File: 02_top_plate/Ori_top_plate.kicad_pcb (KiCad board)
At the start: 2 copper layers, 227.2 x 75.2 mm, 62 parts, among them U1 HOLE, U10 HOLE, U11 HOLE, U12 HOLE, U13 HOLE, U14 HOLE, U15 HOLE, U16 HOLE, U17 HOLE, U18 HOLE, U19 HOLE, U2 HOLE, U20 HOLE, U21 HOLE, U22 HOLE, U23 HOLE, U24 HOLE, U25 HOLE, U26 HOLE, U27 HOLE, U28 HOLE, U29 HOLE, U3 HOLE, U30 HOLE, U31 HOLE, U32 HOLE, U33 HOLE, U34 HOLE, U35 HOLE, U36 HOLE, U37 HOLE, U38 HOLE, U39 HOLE, U4 HOLE, U40 HOLE, U41 HOLE, U42 HOLE, U43 HOLE, U44 HOLE, U45 HOLE, U46 HOLE, U47 HOLE, U48 HOLE, U5 HOLE, U6 HOLE, U7 HOLE, U8 HOLE, U9 HOLE

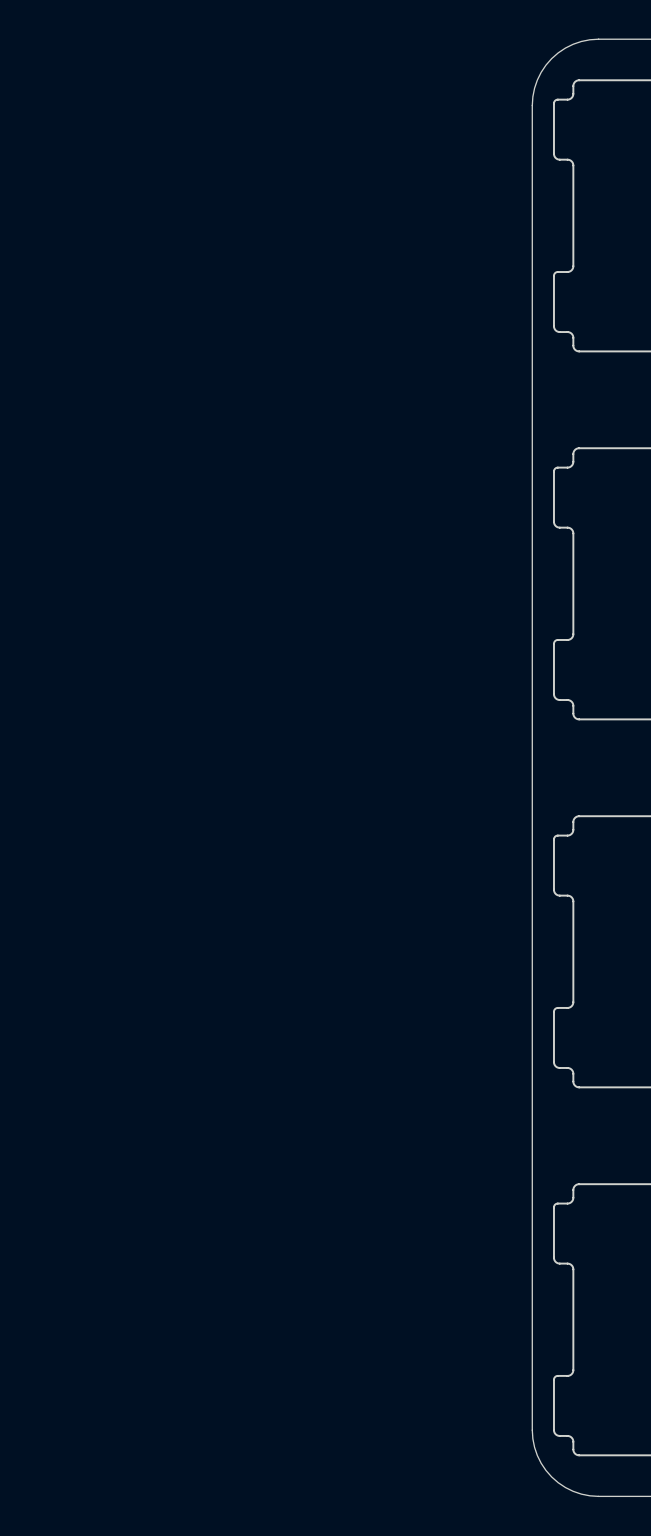
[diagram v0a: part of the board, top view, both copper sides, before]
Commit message: update
added macro column to top plate
re-routed some traces
new previews
removed some ground plane
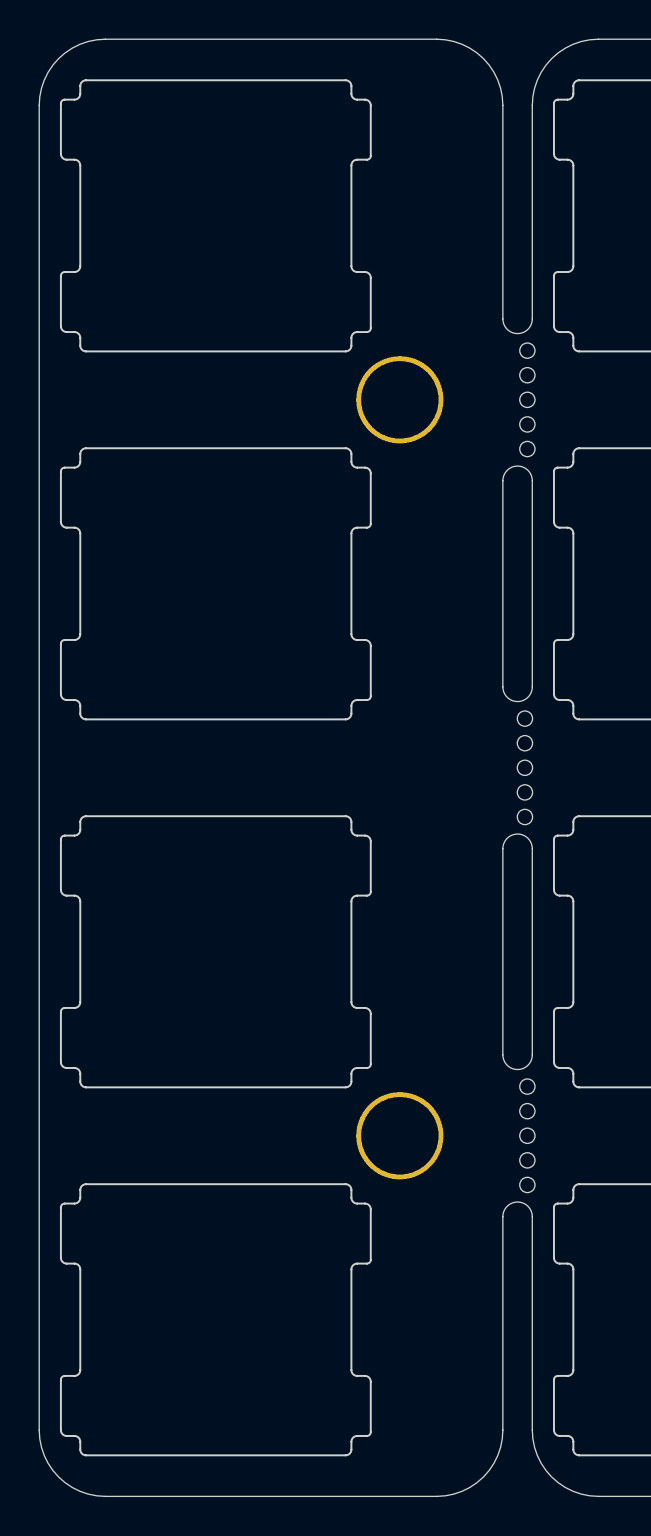
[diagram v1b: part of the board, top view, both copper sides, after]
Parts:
- added H15: MountingHole, random-keyboard-parts:plate_hole_4mm_tht, F.Cu at (124.6, 63.2)
- added H16: MountingHole, random-keyboard-parts:plate_hole_4mm_tht, F.Cu at (124.6, 101.2)
- added H17: MountingHole, random-keyboard-parts:breakaway-mousebites, F.Cu at (131.5, 99.2)
- added H18: MountingHole, random-keyboard-parts:breakaway-mousebites, F.Cu at (131.4, 80.2)
- added H19: MountingHole, random-keyboard-parts:breakaway-mousebites, F.Cu at (131.5, 61.2)
- added U49: HOLE, random-keyboard-parts:MX100_slot, F.Cu at (115.1, 51.7)
- added U50: HOLE, random-keyboard-parts:MX100_slot, F.Cu at (115.1, 70.7)
- added U51: HOLE, random-keyboard-parts:MX100_slot, F.Cu at (115.1, 89.7)
- added U52: HOLE, random-keyboard-parts:MX100_slot, F.Cu at (115.1, 108.7)
- renumbered H14 to H1, H2 to H10, H3 to H11, H6 to H12, H4 to H13, H5 to H14, H15 to H2, H11 to H3, H12 to H4, H13 to H5, H16 to H6, H17 to H7, H18 to H8, H1 to H9
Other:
- board size 227.2 x 75.2 mm -> 252.7 x 75.2 mm

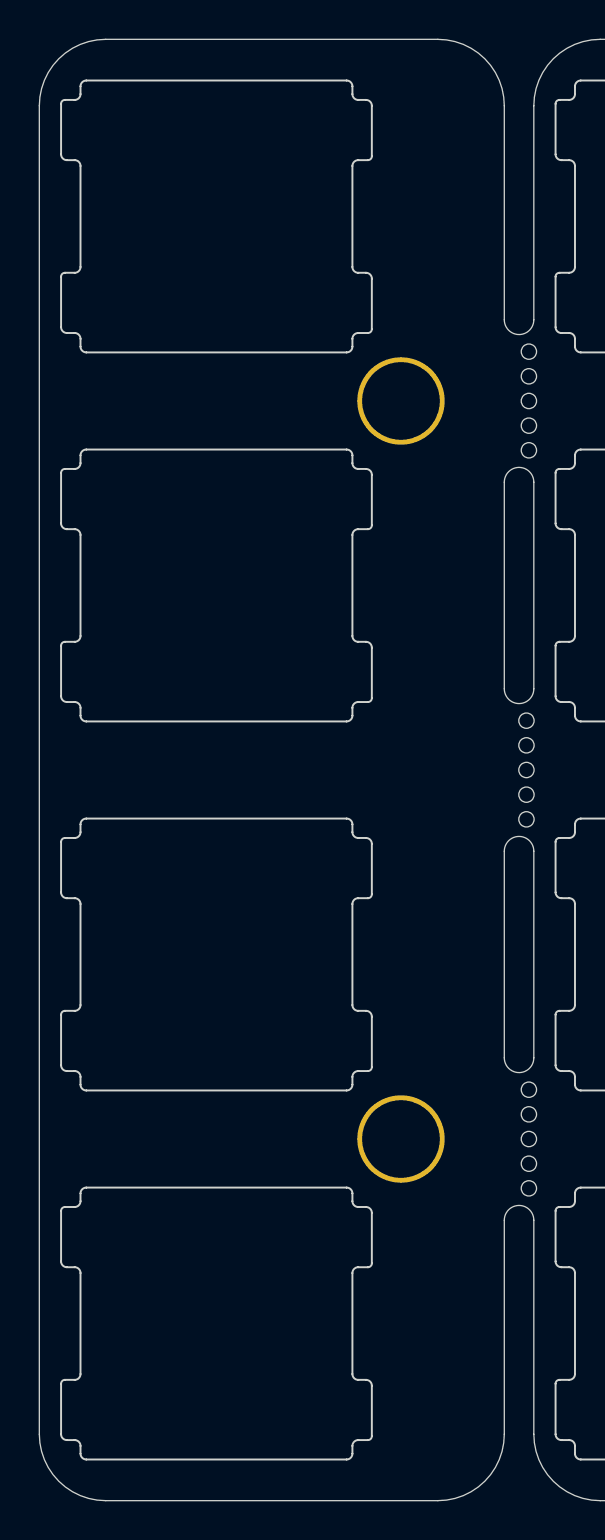
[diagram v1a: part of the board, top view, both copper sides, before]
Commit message: Moved macro column a tiny bit
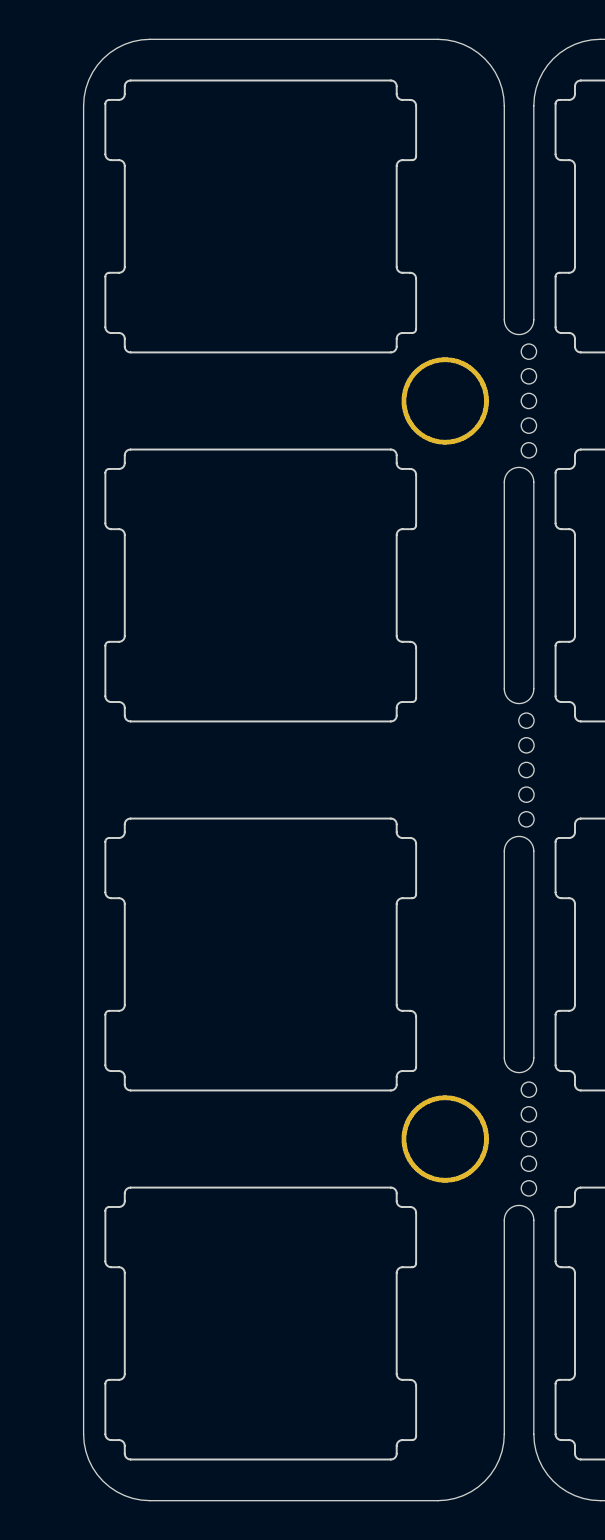
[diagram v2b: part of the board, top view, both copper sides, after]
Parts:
- moved U49 2.28 mm to (117.4, 51.7)
- moved U50 2.28 mm to (117.4, 70.7)
- moved U51 2.28 mm to (117.4, 89.7)
- moved U52 2.28 mm to (117.4, 108.7)
- moved H15 2.28 mm to (126.9, 63.2)
- moved H16 2.28 mm to (126.9, 101.2)
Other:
- board size 252.7 x 75.2 mm -> 250.4 x 75.2 mm
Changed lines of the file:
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@@
   (general
     (thickness 1.6)
-    (drawings 32)
+    (drawings 33)
     (tracks 0)
     (zones 0)
@@
   )
   (module random-keyboard-parts:MX100_slot (layer F.Cu)
-    (at 115.14 108.68)
+    (at 117.419994 108.68)
     (fp_text reference U52 (at 0.0127 1.8288) (layer Dwgs.User)
       (effects (font (size 1 1) (thickness 0.15)))
@@
   )
   (module random-keyboard-parts:MX100_slot (layer F.Cu)
-    (at 115.14 89.68)
+    (at 117.419994 89.68)
     (fp_text reference U51 (at 0.0127 1.8288) (layer Dwgs.User)
       (effects (font (size 1 1) (thickness 0.15)))
@@
   )
   (module random-keyboard-parts:MX100_slot (layer F.Cu)
-    (at 115.14 70.68)
+    (at 117.419994 70.68)
     (fp_text reference U50 (at 0.0127 1.8288) (layer Dwgs.User)
       (effects (font (size 1 1) (thickness 0.15)))
@@
   )
   (module random-keyboard-parts:MX100_slot (layer F.Cu)
-    (at 115.14 51.68)
+    (at 117.419994 51.68)
     (fp_text reference U49 (at 0.0127 1.8288) (layer Dwgs.User)
       (effects (font (size 1 1) (thickness 0.15)))
@@
   )
   (module random-keyboard-parts:plate_hole_4mm_tht (layer F.Cu)
-    (at 124.5892 101.212)
+    (at 126.868866 101.212)
     (fp_text reference H16 (at 0.381 1.4097) (layer Dwgs.User)
       (effects (font (size 1 1) (thickness 0.15)))
@@
   )
   (module random-keyboard-parts:plate_hole_4mm_tht (layer F.Cu)
-    (at 124.5892 63.212)
+    (at 126.868866 63.211839)
     (fp_text reference H15 (at 0.381 1.4097) (layer Dwgs.User)
       (effects (font (size 1 1) (thickness 0.15)))
@@
     (pad 1 thru_hole circle (at 0.0508 -2.032) (size 4.5 4.5) (drill 4) (layers *.Cu *.Mask))
   )
-  (gr_line (start 126.54 117.8) (end 109.44 117.8) (layer Edge.Cuts) (width 0.05))
+  (dimension 4.129636 (width 0.15) (layer Dwgs.User)
+    (gr_text "0.1626 in" (at 129.009495 32.519843 0.001886903836) (layer Dwgs.User)
+      (effects (font (size 1 1) (thickness 0.15)))
+    )
+    (feature1 (pts (xy 126.944994 42.155) (xy 126.9447 33.23349)))
+    (feature2 (pts (xy 131.07463 42.154864) (xy 131.074336 33.233354)))
+    (crossbar (pts (xy 131.074356 33.819775) (xy 126.94472 33.819911)))
+    (arrow1a (pts (xy 126.94472 33.819911) (xy 128.071204 33.233453)))
+    (arrow1b (pts (xy 126.94472 33.819911) (xy 128.071243 34.406295)))
+    (arrow2a (pts (xy 131.074356 33.819775) (xy 129.947833 33.233391)))
+    (arrow2b (pts (xy 131.074356 33.819775) (xy 129.947872 34.406233)))
+  )
+  (dimension 4.129636 (width 0.15) (layer Dwgs.User)
+    (gr_text "4.130 mm" (at 129.009632 36.699832 0.001886903836) (layer Dwgs.User)
+      (effects (font (size 1 1) (thickness 0.15)))
+    )
+    (feature1 (pts (xy 126.944994 42.155) (xy 126.944838 37.413479)))
+    (feature2 (pts (xy 131.07463 42.154864) (xy 131.074474 37.413343)))
+    (crossbar (pts (xy 131.074493 37.999764) (xy 126.944857 37.9999)))
+    (arrow1a (pts (xy 126.944857 37.9999) (xy 128.071341 37.413442)))
+    (arrow1b (pts (xy 126.944857 37.9999) (xy 128.07138 38.586284)))
+    (arrow2a (pts (xy 131.074493 37.999764) (xy 129.94797 37.41338)))
+    (arrow2b (pts (xy 131.074493 37.999764) (xy 129.948009 38.586222)))
+  )
+  (gr_line (start 126.54 117.8) (end 111.719994 117.8) (layer Edge.Cuts) (width 0.05))
   (gr_line (start 129.96 114.38) (end 129.96 103.36) (layer Edge.Cuts) (width 0.05))
   (gr_arc (start 126.54 114.38) (end 126.54 117.8) (angle -90) (layer Edge.Cuts) (width 0.05))
@@
   (gr_line (start 129.96 45.98) (end 129.96 57) (layer Edge.Cuts) (width 0.05))
   (gr_line (start 131.48 45.98) (end 131.48 57) (layer Edge.Cuts) (width 0.05))
-  (gr_line (start 126.54 42.56) (end 109.44 42.56) (layer Edge.Cuts) (width 0.05))
+  (gr_line (start 126.54 42.56) (end 111.719994 42.56) (layer Edge.Cuts) (width 0.05))
   (gr_arc (start 130.72 57) (end 129.96 57) (angle -180) (layer Edge.Cuts) (width 0.05))
   (gr_arc (start 126.54 45.98) (end 129.96 45.98) (angle -90) (layer Edge.Cuts) (width 0.05))
-  (gr_line (start 106.02 45.98) (end 106.02 114.38) (layer Edge.Cuts) (width 0.05))
-  (gr_arc (start 109.44 45.98) (end 109.44 42.56) (angle -90) (layer Edge.Cuts) (width 0.05))
-  (gr_arc (start 109.44 114.38) (end 106.02 114.38) (angle -90) (layer Edge.Cuts) (width 0.05))
-  (dimension 6.40963 (width 0.15) (layer Cmts.User)
-    (gr_text "0.2523 in" (at 127.869691 36.31994 0.001215706057) (layer Cmts.User)
-      (effects (font (size 1 1) (thickness 0.15)))
-    )
-    (feature1 (pts (xy 124.665 42.155) (xy 124.664891 37.033587)))
-    (feature2 (pts (xy 131.07463 42.154864) (xy 131.074521 37.033451)))
-    (crossbar (pts (xy 131.074534 37.619872) (xy 124.664904 37.620008)))
-    (arrow1a (pts (xy 124.664904 37.620008) (xy 125.791395 37.033563)))
-    (arrow1b (pts (xy 124.664904 37.620008) (xy 125.79142 38.206405)))
-    (arrow2a (pts (xy 131.074534 37.619872) (xy 129.948018 37.033475)))
-    (arrow2b (pts (xy 131.074534 37.619872) (xy 129.948043 38.206317)))
-  )
+  (gr_line (start 108.299994 45.98) (end 108.299994 114.38) (layer Edge.Cuts) (width 0.05))
+  (gr_arc (start 111.719994 45.98) (end 111.719994 42.56) (angle -90) (layer Edge.Cuts) (width 0.05))
+  (gr_arc (start 111.719994 114.38) (end 108.299994 114.38) (angle -90) (layer Edge.Cuts) (width 0.05))
   (gr_text github.com/dierickdie (at 245.099355 61.179839) (layer B.SilkS)
     (effects (font (size 1.5 1.5) (thickness 0.2)) (justify mirror))

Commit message: 19.05mm spacing; move macro column to right side
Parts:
- removed H10, H11, H12, H13, H14, H9: MountingHole, random-keyboard-parts:plate_hole_4mm_tht
- added D1: DIODE, Diode_SMD:D_0603_1608Metric_Pad1.05x0.95mm_HandSolder, B.Cu at (374.5, 60.7)
- added D2: DIODE, Diode_SMD:D_0603_1608Metric_Pad1.05x0.95mm_HandSolder, B.Cu at (350.0, 60.7)
- moved U49 256.4 mm to (373.9, 51.2)
- moved U50 256.4 mm to (373.9, 70.2)
- moved U51 256.4 mm to (373.9, 89.3)
- moved U52 256.4 mm to (373.9, 108.3)
- moved H15 237.4 mm to (364.3, 62.8)
- moved H16 237.4 mm to (364.3, 100.9)
- moved H18 227.9 mm to (359.2, 79.8)
- moved H19 227.7 mm to (359.2, 60.7)
- moved H17 227.7 mm to (359.2, 98.8)
- moved U12 0.66 mm to (350.0, 51.2)
- moved U11 0.62 mm to (331.0, 51.2)
- moved U24 0.62 mm to (350.0, 70.2)
- moved H7 0.62 mm to (340.5, 62.8)
- moved U10 0.59 mm to (311.9, 51.2)
- moved U36 0.59 mm to (350.0, 89.3)
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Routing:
- net GNDA: track 0.00 -> 1.51 mm, vias 0 -> 1
- net GND: track 0.00 -> 1.51 mm, vias 0 -> 1
- added copper zone on B.Cu, net GND
- added copper zone on F.Cu, net GND
- added copper zone on B.Cu, net GNDA
- added copper zone on F.Cu, net GNDA
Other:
- board size 250.4 x 75.2 mm -> 251.2 x 75 mm

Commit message: updated plate holes
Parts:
- H17, H18, H19: footprint random-keyboard-parts:breakaway-mousebites -> Keeb_footprints:MouseBite_IPC7351
- U1, U10, U11, U12, U13, U14, U15, U16, U17, U18, U19, U2, U20, U21, U22, U23, U24, U25, U26, U27, U28, U29, U3, U30, U31, U32, U33, U34, U35, U36, U37, U38, U39, U4, U40, U41, U42, U43, U44, U45, U46, U47, U48, U49, U5, U50, U51, U52, U6, U7, U8, U9: footprint random-keyboard-parts:MX100_slot -> Keebio-Parts:MX_Switch_Cutout

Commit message: Updated firmware
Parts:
- removed H17: MountingHole, Keeb_footprints:MouseBite_IPC7351
- removed U50, U51, U52: HOLE, Keebio-Parts:MX_Switch_Cutout
- added H10: MountingHole, random-keyboard-parts:Generic-Mounthole, F.Cu at (222.6, 59.5)
- added H11: MountingHole, random-keyboard-parts:Generic-Mounthole, F.Cu at (222.6, 97.6)
- added H12: MountingHole, random-keyboard-parts:Generic-Mounthole, F.Cu at (297.9, 59.7)
- added H13: MountingHole, random-keyboard-parts:Generic-Mounthole, F.Cu at (298.8, 97.6)
- added H14: MountingHole, random-keyboard-parts:Generic-Mounthole, F.Cu at (356.0, 59.5)
- added H20: MountingHole, acheron_Hardware:MouseBite_IPC7351, F.Cu at (375.0, 78.6)
- added H21: MountingHole, random-keyboard-parts:Generic-Mounthole, F.Cu at (389.4, 39.9)
- added H22: MountingHole, random-keyboard-parts:Generic-Mounthole, F.Cu at (389.4, 117.3)
- added H9: MountingHole, random-keyboard-parts:Generic-Mounthole, F.Cu at (165.5, 59.5)
- added U53: HOLE, Keeb_footprints:MX100_slot, F.Cu at (389.4, 69.0)
- added U57: HOLE, Keeb_footprints:MX100_slot, F.Cu at (389.4, 88.1)
- added U61: HOLE, Keeb_footprints:MX100_slot, F.Cu at (389.3, 107.2)
- D1, D2: footprint Diode_SMD:D_0603_1608Metric_Pad1.05x0.95mm_HandSolder -> Keeb_footprints:D_SOD-123_modified; moved to F.Cu
- H1, H15, H16, H2, H3, H4, H5, H6, H7, H8: footprint random-keyboard-parts:plate_hole_4mm_tht -> random-keyboard-parts:Generic-Mounthole
- H18, H19: footprint Keeb_footprints:MouseBite_IPC7351 -> acheron_Hardware:MouseBite_IPC7351
- U1, U10, U11, U12, U13, U14, U15, U16, U17, U18, U19, U2, U20, U21, U22, U23, U24, U25, U26, U27, U28, U29, U3, U30, U31, U32, U33, U34, U35, U36, U37, U38, U39, U4, U40, U41, U42, U43, U44, U45, U46, U47, U48, U49, U5, U6, U7, U8, U9: footprint Keebio-Parts:MX_Switch_Cutout -> Keeb_footprints:MX100_slot
- moved H8 175.0 mm to (165.5, 97.6)
- moved H6 149.8 mm to (356.0, 117.3)
- moved H2 118.9 mm to (165.5, 117.3)
- moved H3 113.1 mm to (260.8, 39.9)
- moved H4 112.0 mm to (260.8, 117.3)
- moved H5 76.2 mm to (356.0, 39.9)
- moved H7 52.6 mm to (379.8, 97.7)
- moved H1 47.5 mm to (165.5, 39.9)
- moved H16 44.2 mm to (379.8, 59.5)
- moved H19 40.2 mm to (375.0, 97.6)
- moved H15 35.8 mm to (356.0, 97.6)
- moved H18 25.7 mm to (375.0, 59.5)
- moved D2 19.1 mm to (369.1, 59.5)
- moved U12 15.5 mm to (365.5, 50.0)
- moved U21 15.5 mm to (308.4, 69.1)
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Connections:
- D1 pad 2: GND -> GND1
- D2 pad 2: GNDA -> GND
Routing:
- net GND1: track 0.00 -> 2.52 mm, vias 0 -> 1
- net GNDA: track 1.51 -> 0.00 mm, vias 1 -> 0
- net GND: track 1.51 -> 2.52 mm
- added copper zone on B.Cu, net GND1
- added copper zone on F.Cu, net GND1
- removed copper zone on B.Cu, net GNDA
- removed copper zone on F.Cu, net GNDA
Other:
- board size 251.2 x 75 mm -> 252.4 x 82.2 mm
- net class Default: clearance 0.2 -> 0.13; via_dia 0.8 -> 0.5; via_drill 0.4 -> 0.25
- net class Thick added: clearance 0.13, trace_width 0.5, via_dia 0.8, via_drill 0.5
- rule pad_to_mask_clearance: 0.051 -> 0
- rule trace_clearance: 0.2 -> 0.13
- rule trace_min: 0.2 -> 0.13
- rule via_min_drill: 0.3 -> 0.25
- rule via_min_size: 0.4 -> 0.5
